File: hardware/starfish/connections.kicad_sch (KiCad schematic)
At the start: 23 parts, among them J401 Cam LED, J402 Aux out, J403 Voltage, J404 Inputs, J405 Qwiic, J406 Qwiic, J407 USB B, U401 74HC2G34, U402 74HC2G34, U403 TVS

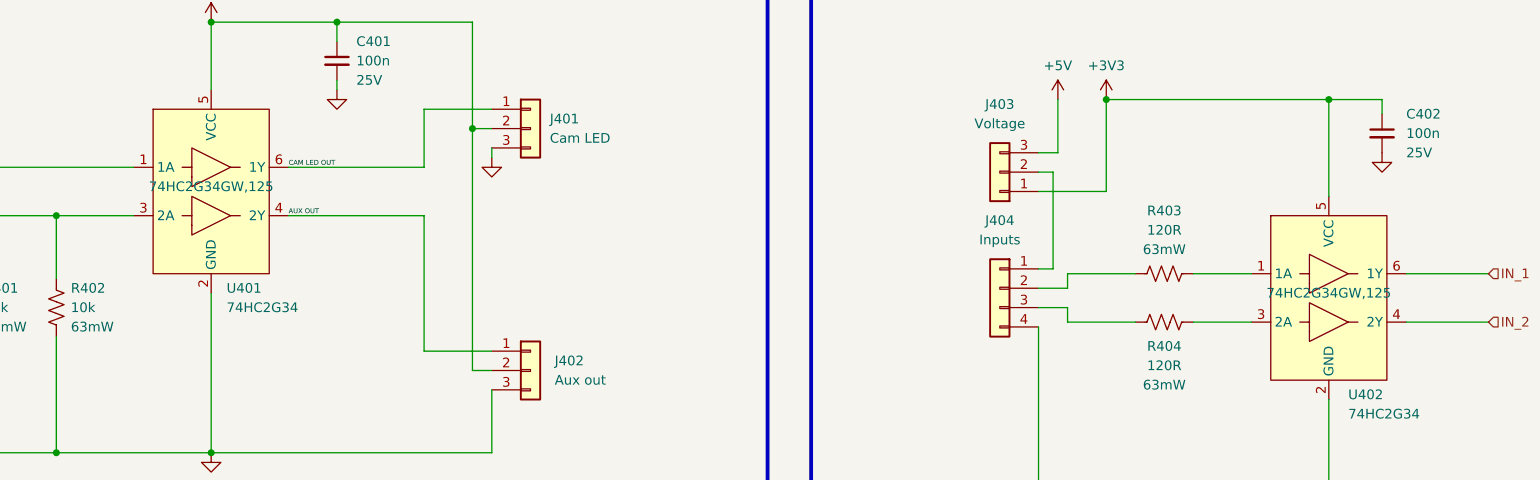
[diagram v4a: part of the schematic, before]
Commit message: Run through purchasing, update some cap sizes
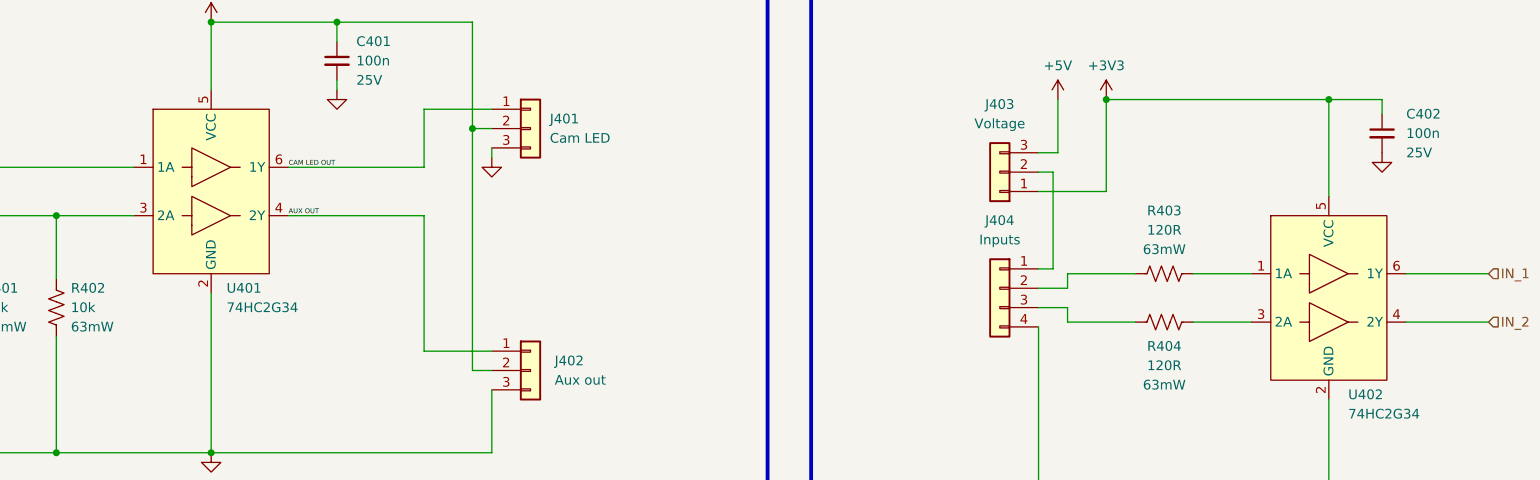
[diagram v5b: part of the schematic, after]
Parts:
- D401, D402, D403, D404: MPN PESD5V0U1BA,115 -> (none); Notes DOUBLE CHECK FOOTPRINT -> (none); mpn PESD5V0X1BT,215 -> PESD5V0U1BA,115
- J403: mpn (none) -> BHR-06-VUA
- R403, R404: mpn (none) -> CRGCQ0402F120R
- U401, U402: MPN 74HC2G34GW,125 -> (none)
- U403: mpn SRL05-TP -> SRL05-TP, 82400102
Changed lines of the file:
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@@
       (effects (font (size 1.27 1.27)) hide)
     )
-    (property "mpn" "PESD5V0X1BT,215" (id 4) (at 62.865 178.435 0)
+    (property "mpn" "PESD5V0U1BA,115" (id 4) (at 62.865 178.435 0)
       (effects (font (size 1.27 1.27)) hide)
     )
@@
       (effects (font (size 1.27 1.27)) hide)
     )
-    (property "Notes" "DOUBLE CHECK FOOTPRINT" (id 6) (at 62.865 178.435 0)
-      (effects (font (size 1.27 1.27)) hide)
-    )
-    (property "MPN" "PESD5V0U1BA,115" (id 7) (at 62.865 178.435 0)
+    (property "Notes" "" (id 6) (at 62.865 178.435 0)
+      (effects (font (size 1.27 1.27)) hide)
+    )
+    (property "MPN" "" (id 7) (at 62.865 178.435 0)
       (effects (font (size 1.27 1.27)) hide)
     )
@@
       (effects (font (size 1.27 1.27)) hide)
     )
-    (property "mpn" "" (id 4) (at 193.675 70.485 0)
+    (property "mpn" "CRGCQ0402F120R" (id 4) (at 193.675 70.485 0)
       (effects (font (size 1.27 1.27)) hide)
     )
@@
       (effects (font (size 1.27 1.27)) hide)
     )
-    (property "mpn" "PESD5V0X1BT,215" (id 4) (at 76.2 178.435 0)
+    (property "mpn" "PESD5V0U1BA,115" (id 4) (at 76.2 178.435 0)
       (effects (font (size 1.27 1.27)) hide)
     )
@@
       (effects (font (size 1.27 1.27)) hide)
     )
-    (property "Notes" "DOUBLE CHECK FOOTPRINT" (id 6) (at 76.2 178.435 0)
-      (effects (font (size 1.27 1.27)) hide)
-    )
-    (property "MPN" "PESD5V0U1BA,115" (id 7) (at 76.2 178.435 0)
+    (property "Notes" "" (id 6) (at 76.2 178.435 0)
+      (effects (font (size 1.27 1.27)) hide)
+    )
+    (property "MPN" "" (id 7) (at 76.2 178.435 0)
       (effects (font (size 1.27 1.27)) hide)
     )
@@
       (effects (font (size 1.27 1.27)) hide)
     )
-    (property "mpn" "PESD5V0X1BT,215" (id 4) (at 76.2 137.16 0)
+    (property "mpn" "PESD5V0U1BA,115" (id 4) (at 76.2 137.16 0)
       (effects (font (size 1.27 1.27)) hide)
     )
@@
       (effects (font (size 1.27 1.27)) hide)
     )
-    (property "Notes" "DOUBLE CHECK FOOTPRINT" (id 6) (at 76.2 137.16 0)
-      (effects (font (size 1.27 1.27)) hide)
-    )
-    (property "MPN" "PESD5V0U1BA,115" (id 7) (at 76.2 137.16 0)
+    (property "Notes" "" (id 6) (at 76.2 137.16 0)
+      (effects (font (size 1.27 1.27)) hide)
+    )
+    (property "MPN" "" (id 7) (at 76.2 137.16 0)
       (effects (font (size 1.27 1.27)) hide)
     )
@@
       (effects (font (size 1.27 1.27)) hide)
     )
-    (property "mpn" "PESD5V0X1BT,215" (id 4) (at 62.865 137.16 0)
+    (property "mpn" "PESD5V0U1BA,115" (id 4) (at 62.865 137.16 0)
       (effects (font (size 1.27 1.27)) hide)
     )
@@
       (effects (font (size 1.27 1.27)) hide)
     )
-    (property "Notes" "DOUBLE CHECK FOOTPRINT" (id 6) (at 62.865 137.16 0)
-      (effects (font (size 1.27 1.27)) hide)
-    )
-    (property "MPN" "PESD5V0U1BA,115" (id 7) (at 62.865 137.16 0)
+    (property "Notes" "" (id 6) (at 62.865 137.16 0)
+      (effects (font (size 1.27 1.27)) hide)
+    )
+    (property "MPN" "" (id 7) (at 62.865 137.16 0)
       (effects (font (size 1.27 1.27)) hide)
     )
@@
       (effects (font (size 1.27 1.27)) (justify left) hide)
     )
-    (property "MPN" "74HC2G34GW,125" (id 5) (at 68.58 52.705 0))
+    (property "MPN" "" (id 5) (at 68.58 52.705 0))
     (pin "1")
     (pin "2")
@@
       (effects (font (size 1.27 1.27)) hide)
     )
+    (property "mpn" "BHR-06-VUA" (id 4) (at 172.085 50.8 0)
+      (effects (font (size 1.27 1.27)) hide)
+    )
     (pin "1")
     (pin "2")
@@
       (effects (font (size 1.27 1.27)) hide)
     )
-    (property "mpn" "" (id 4) (at 193.675 64.135 0)
+    (property "mpn" "CRGCQ0402F120R" (id 4) (at 193.675 64.135 0)
       (effects (font (size 1.27 1.27)) hide)
     )
@@
       (effects (font (size 1.27 1.27)) hide)
     )
-    (property "mpn" "SRL05-TP" (id 4) (at 222.25 174.625 0)
+    (property "mpn" "SRL05-TP, 82400102" (id 4) (at 222.25 174.625 0)
       (effects (font (size 1.27 1.27)) hide)
     )
@@
       (effects (font (size 1.27 1.27)) (justify left) hide)
     )
-    (property "MPN" "74HC2G34GW,125" (id 5) (at 215.265 66.675 0))
-    (pin "1")
-    (pin "2")
+    (property "MPN" "" (id 5) (at 215.265 66.675 0))
+    (pin "1")
+    (pin "2")
